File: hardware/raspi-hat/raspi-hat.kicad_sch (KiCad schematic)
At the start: 1 part, among them J2 Conn_01x03_Pin

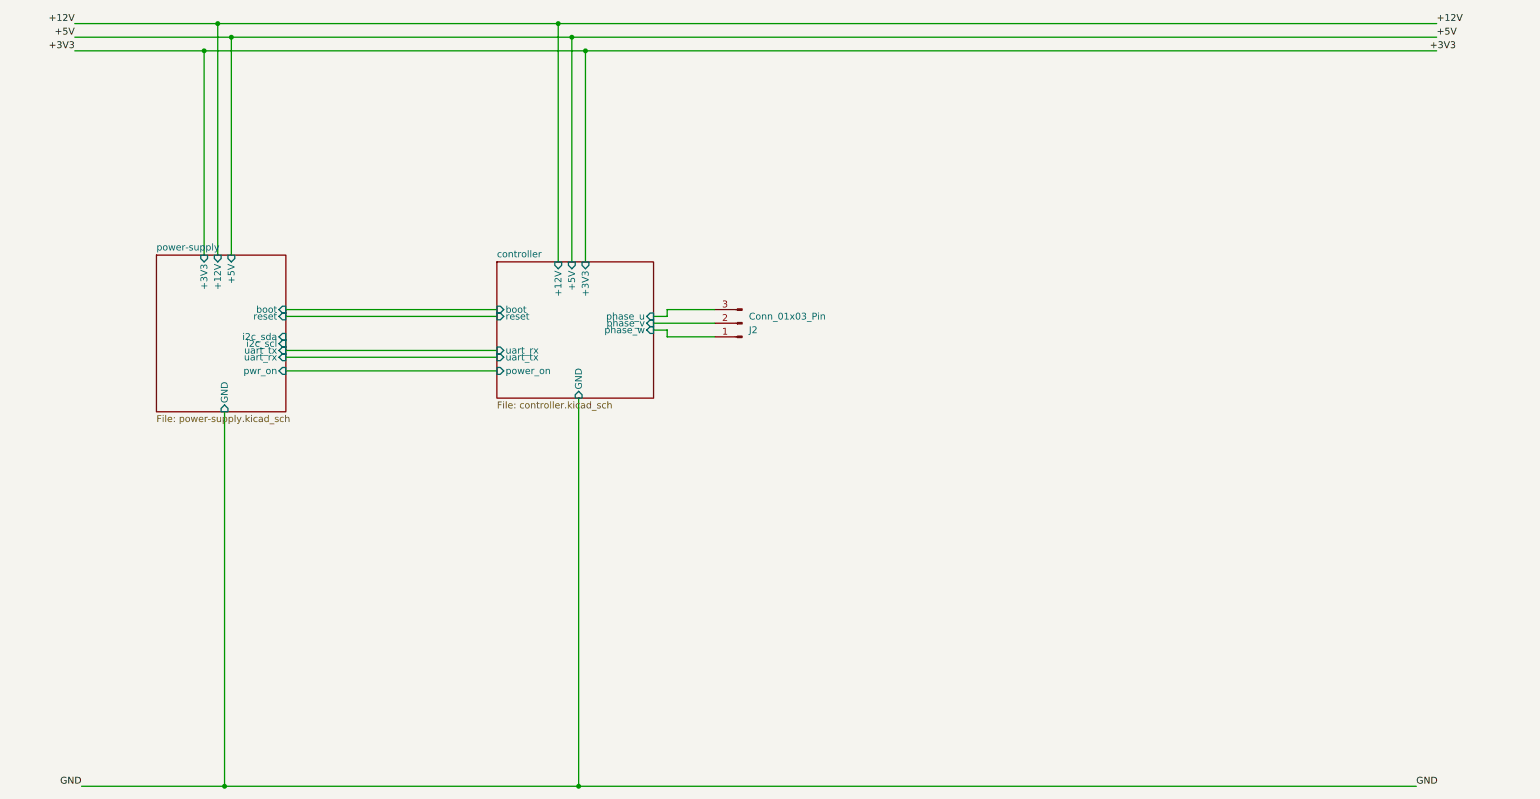
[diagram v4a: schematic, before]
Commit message: - some readability improvements - some routing updates
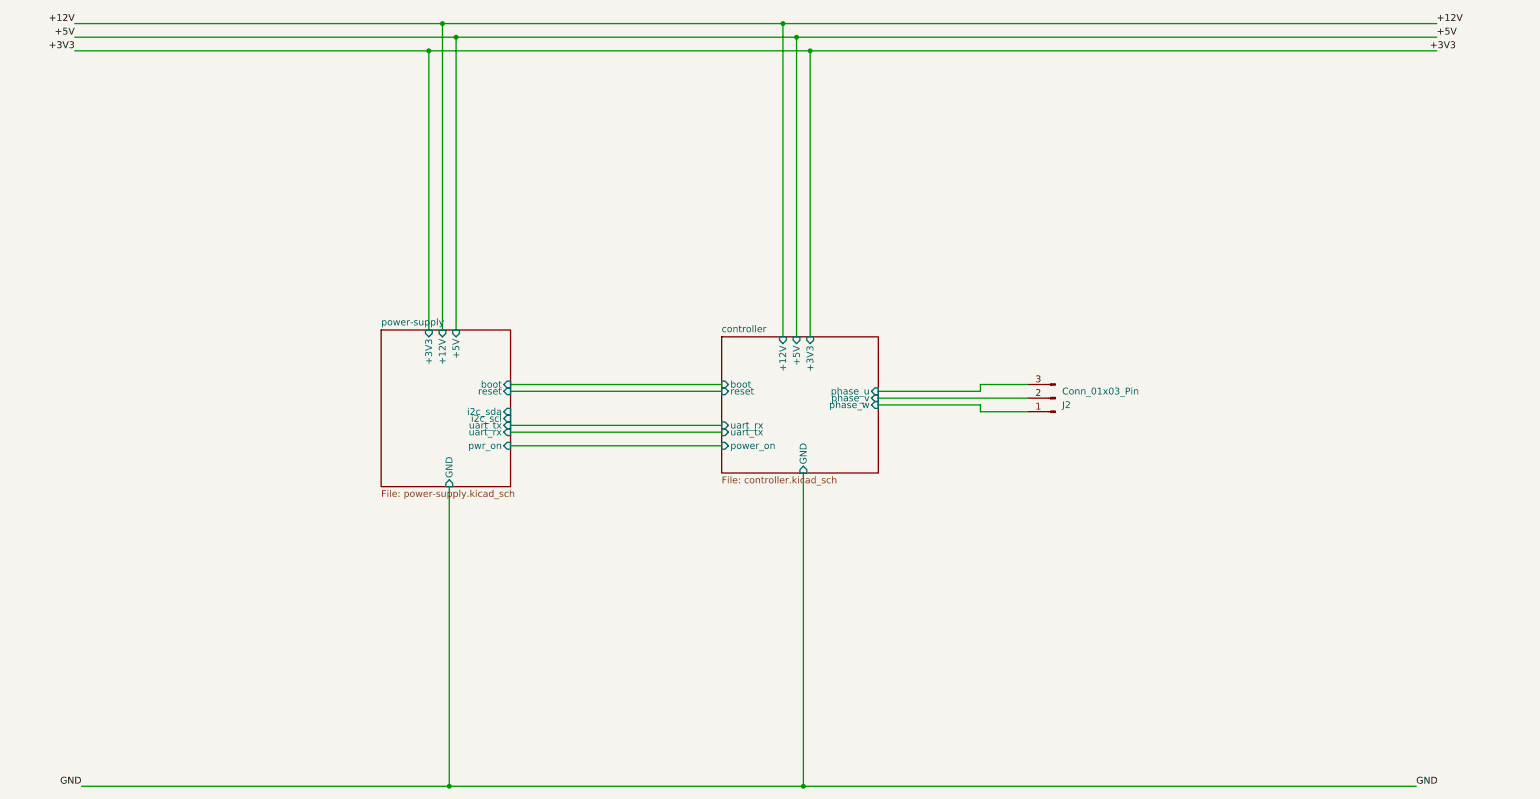
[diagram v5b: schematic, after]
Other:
- moved on the sheet: J2

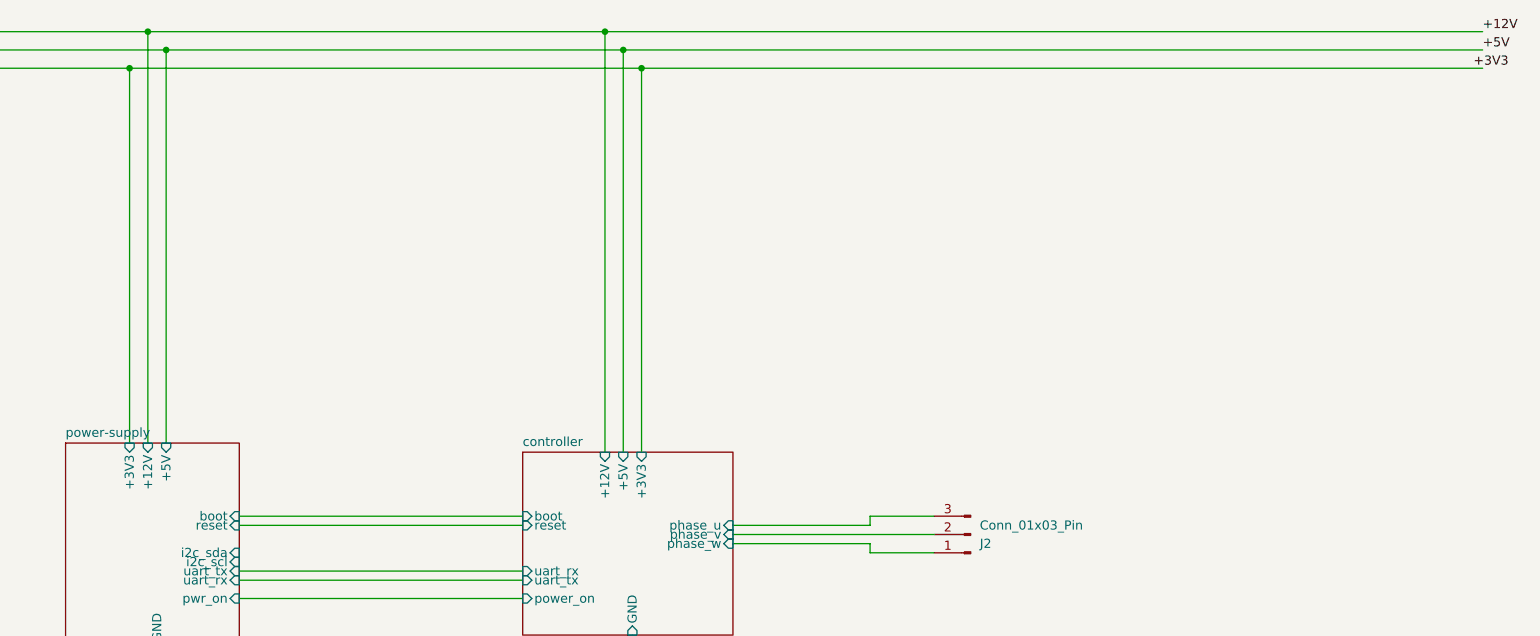
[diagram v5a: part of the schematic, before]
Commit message: replaced usb connector for hall sensors with usbc
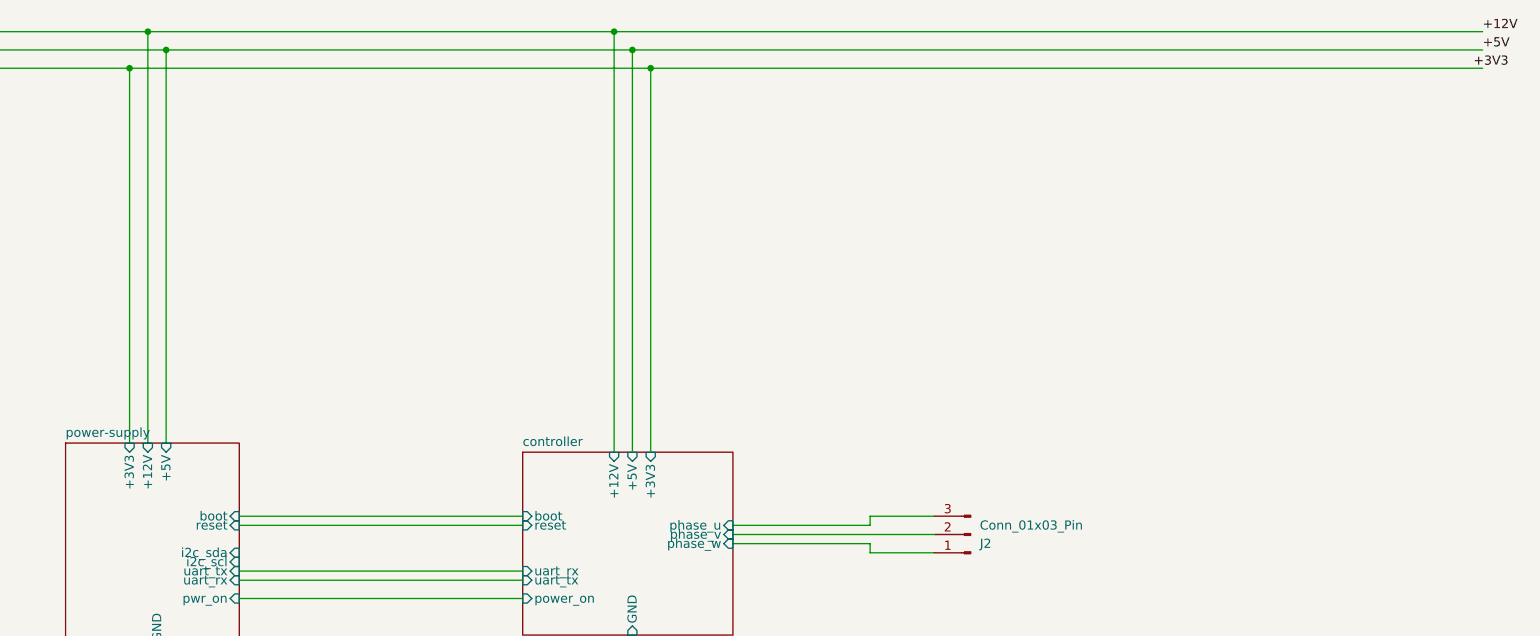
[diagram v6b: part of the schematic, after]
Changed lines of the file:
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@@
 	(paper "A4")
+	(junction
+		(at 161.29 24.13)
+		(diameter 0)
+		(color 0 0 0 0)
+	)
 	(junction
 		(at 93.98 21.59)
@@
 	)
 	(junction
-		(at 154.94 19.05)
+		(at 92.71 161.29)
 		(diameter 0)
 		(color 0 0 0 0)
 	)
 	(junction
-		(at 92.71 161.29)
+		(at 158.75 21.59)
 		(diameter 0)
 		(color 0 0 0 0)
@@
 	)
 	(junction
-		(at 160.02 24.13)
-		(diameter 0)
-		(color 0 0 0 0)
-	)
-	(junction
-		(at 157.48 21.59)
+		(at 156.21 19.05)
 		(diameter 0)
 		(color 0 0 0 0)
@@
 	(wire
 		(pts
-			(xy 88.9 24.13) (xy 160.02 24.13)
+			(xy 88.9 24.13) (xy 161.29 24.13)
 		)
 		(stroke
@@
 	(wire
 		(pts
-			(xy 154.94 19.05) (xy 276.86 19.05)
-		)
-		(stroke
-			(width 0)
-			(type default)
-		)
-	)
-	(wire
-		(pts
 			(xy 158.75 102.87) (xy 158.75 161.29)
 		)
@@
 	(wire
 		(pts
-			(xy 93.98 21.59) (xy 157.48 21.59)
+			(xy 93.98 21.59) (xy 158.75 21.59)
 		)
 		(stroke
@@
 	(wire
 		(pts
-			(xy 160.02 24.13) (xy 276.86 24.13)
-		)
-		(stroke
-			(width 0)
-			(type default)
-		)
-	)
-	(wire
-		(pts
-			(xy 160.02 24.13) (xy 160.02 77.47)
+			(xy 161.29 24.13) (xy 161.29 77.47)
+		)
+		(stroke
+			(width 0)
+			(type default)
+		)
+	)
+	(wire
+		(pts
+			(xy 158.75 21.59) (xy 276.86 21.59)
 		)
 		(stroke
@@
 	(wire
 		(pts
-			(xy 157.48 21.59) (xy 276.86 21.59)
-		)
-		(stroke
-			(width 0)
-			(type default)
-		)
-	)
-	(wire
-		(pts
 			(xy 191.77 87.63) (xy 172.72 87.63)
 		)
@@
 	(wire
 		(pts
-			(xy 157.48 21.59) (xy 157.48 77.47)
+			(xy 156.21 19.05) (xy 276.86 19.05)
+		)
+		(stroke
+			(width 0)
+			(type default)
+		)
+	)
+	(wire
+		(pts
+			(xy 158.75 21.59) (xy 158.75 77.47)
 		)
 		(stroke
@@
 	(wire
 		(pts
-			(xy 91.44 19.05) (xy 154.94 19.05)
+			(xy 91.44 19.05) (xy 156.21 19.05)
 		)
 		(stroke
@@
 	(wire
 		(pts
-			(xy 154.94 19.05) (xy 154.94 77.47)
+			(xy 156.21 19.05) (xy 156.21 77.47)
 		)
 		(stroke
@@
 		(pts
 			(xy 191.77 91.44) (xy 200.66 91.44)
+		)
+		(stroke
+			(width 0)
+			(type default)
+		)
+	)
+	(wire
+		(pts
+			(xy 161.29 24.13) (xy 276.86 24.13)
 		)
 		(stroke
@@
 		)
 		(pin "+3V3" input
-			(at 160.02 77.47 90)
+			(at 161.29 77.47 90)
 			(effects
 				(font
@@
 		)
 		(pin "+12V" input
-			(at 154.94 77.47 90)
+			(at 156.21 77.47 90)
 			(effects
 				(font
@@
 		)
 		(pin "+5V" input
-			(at 157.48 77.47 90)
-			(effects
-				(font
+			(at 158.75 77.47 90)
+			(effects
+				(font
